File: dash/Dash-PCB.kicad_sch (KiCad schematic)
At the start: 91 parts, among them IC1 HT16K33, IC2 TLV62130ARGTT, J1 IO, J2 Conn_01x05_Pin, J3 Conn_02x06_Counter_Clockwise, Q1 XP262N7002TR-G, Q2 XP262N7002TR-G, Q3 XP262N7002TR-G, Q4 XP262N7002TR-G, U1 PIC18F47Q84-I/PT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

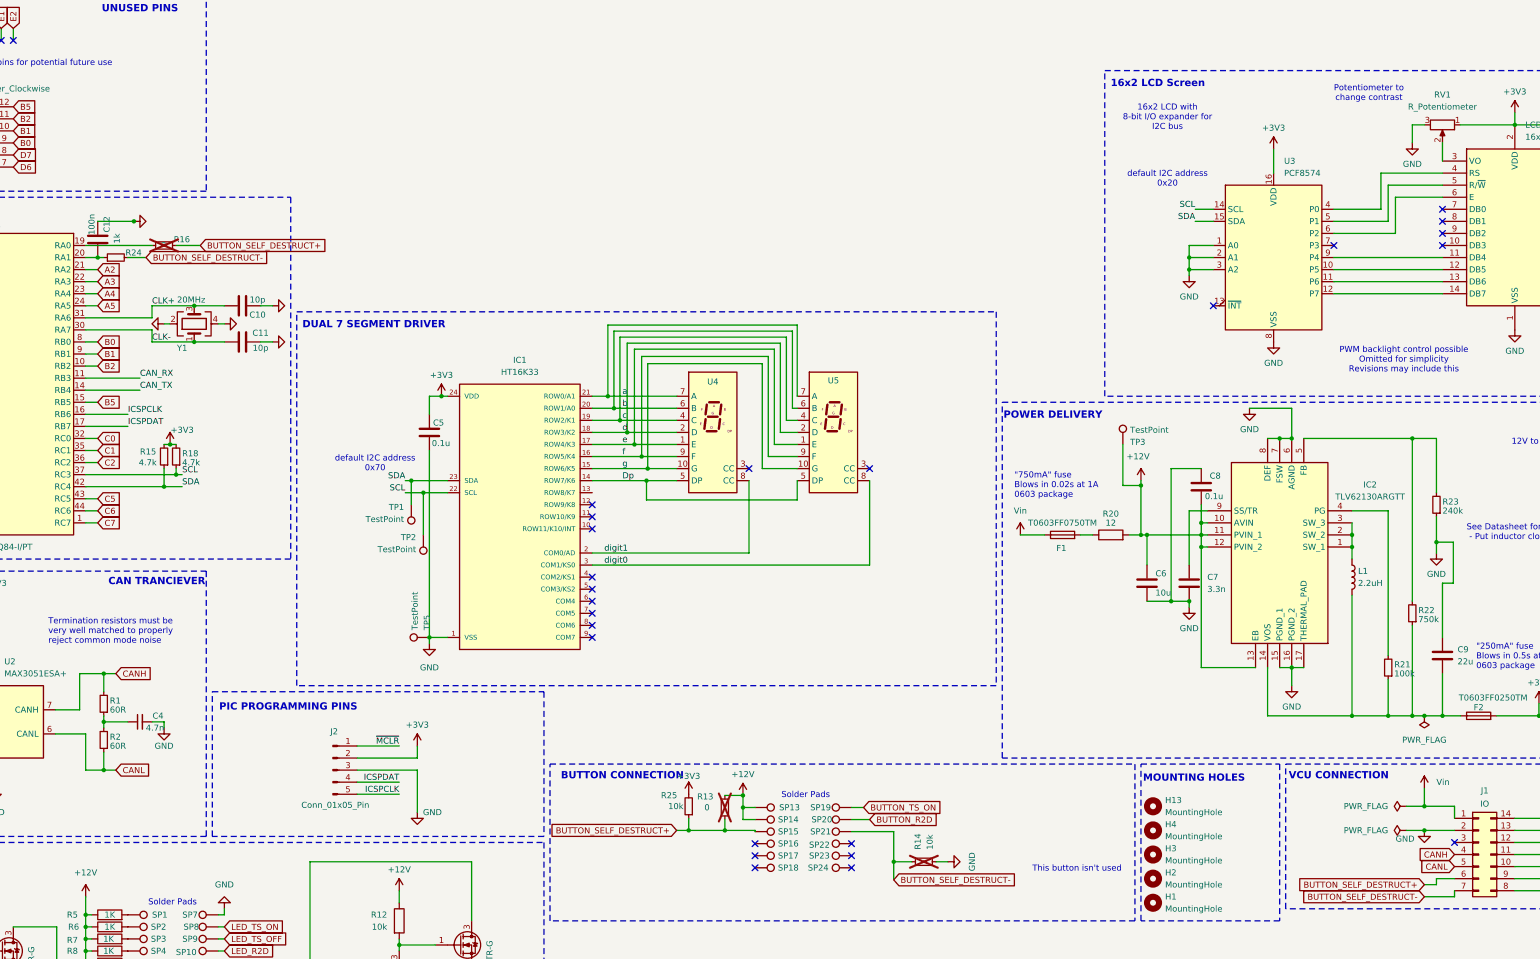
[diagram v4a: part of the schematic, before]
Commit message: Tweaked PCB
Moved CAN X-ver to back, neatened and shortened traces
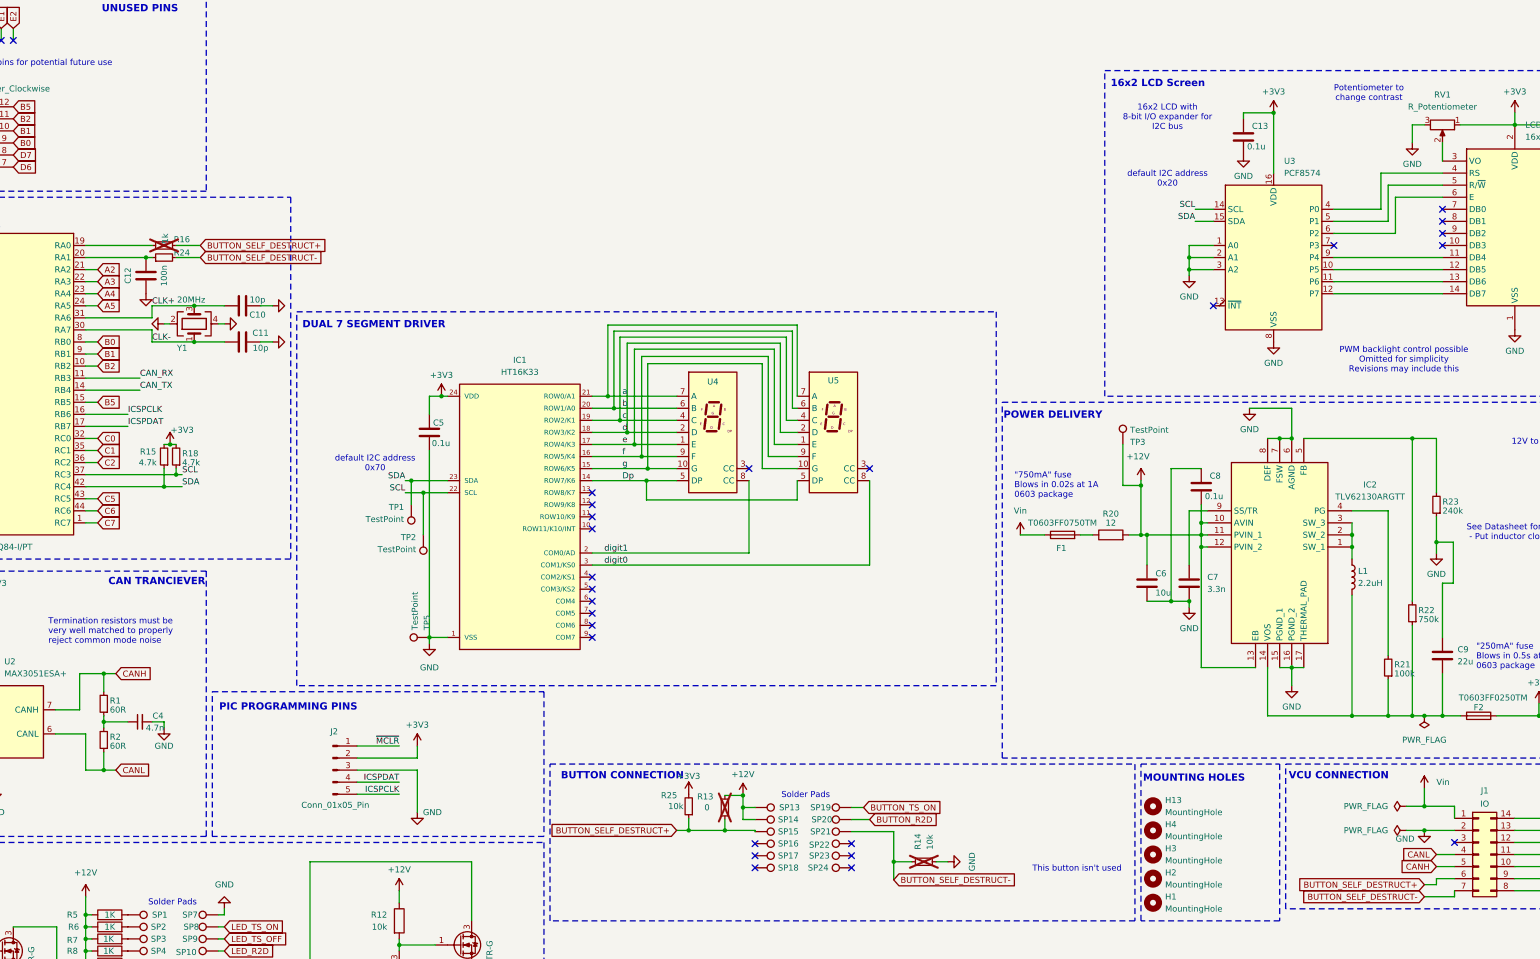
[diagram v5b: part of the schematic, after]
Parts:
- added C13: 0.1u, Capacitor_SMD:C_0805_2012Metric_Pad1.18x1.45mm_HandSolder, symbol Device:C
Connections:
- net +3V3: now also C13.1
- net CANH: now also J1.5 (Pin_5); no longer J1.4 (Pin_4)
- net CANL: now also J1.4 (Pin_4); no longer J1.5 (Pin_5)
- net GND: now also C13.2
- no-connect marks 42 -> 43
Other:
- moved on the sheet: C12, R24

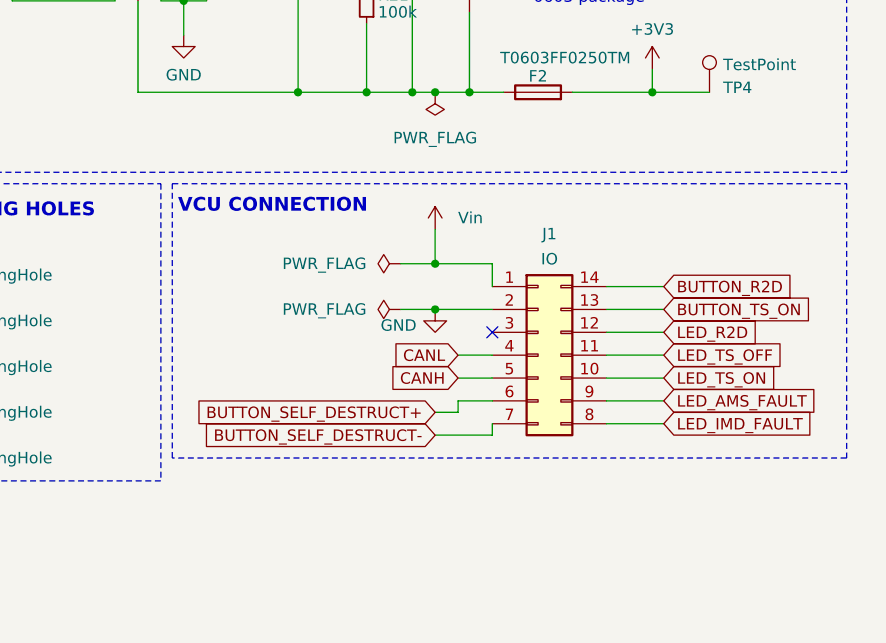
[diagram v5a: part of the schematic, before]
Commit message: button debounce circuit fixed and solder jumpers added
Solder jumpers added to self destruct button's vcu connection. This is because when the button is used for changing lcd information, it has nothing to do with the VCU so needs no connection. Also prevents the VCU accidentally damaging the dash board through these pins.

Also, minor silkscreen placement improvements.
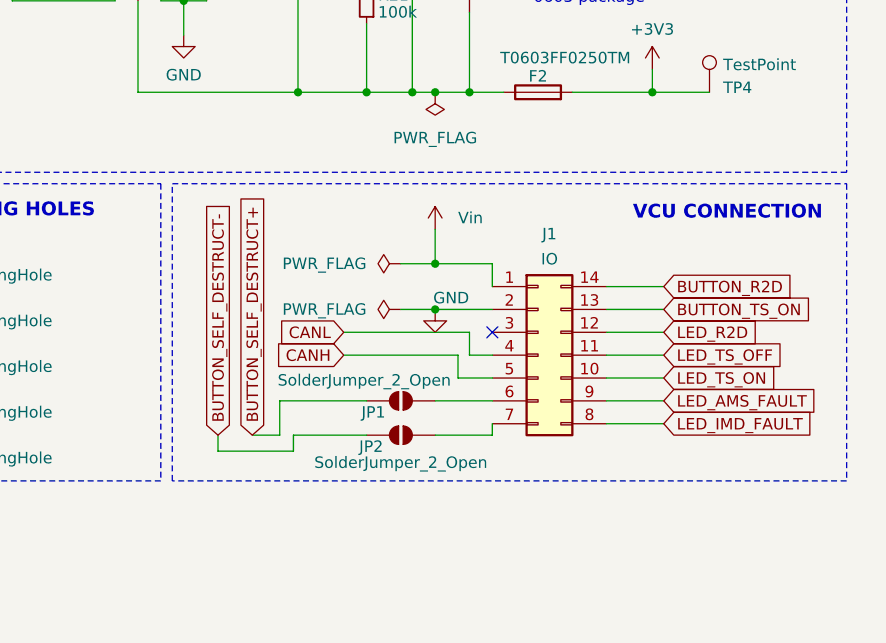
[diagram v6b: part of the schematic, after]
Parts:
- added JP1, JP2: SolderJumper_2_Open, symbol Jumper:SolderJumper_2_Open
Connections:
- net BUTTON_SELF_DESTRUCT+: now also JP1.1 (A); no longer J1.6 (Pin_6)
- net BUTTON_SELF_DESTRUCT-: now also JP2.1 (A); no longer J1.7 (Pin_7)
- new net: J1.6 (Pin_6), JP1.2 (B)
- new net: J1.7 (Pin_7), JP2.2 (B)

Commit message: forgot to commit schematic
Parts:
- JP1, JP2: footprint (none) -> Jumper:SolderJumper-2_P1.3mm_Open_TrianglePad1.0x1.5mm
- R14: value 10k -> 0; now fitted
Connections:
- net BUTTON_SELF_DESTRUCT+: now also R24.2; no longer R16.2
- net BUTTON_SELF_DESTRUCT-: now also R16.2; no longer R24.2
- net at U1.19 (RA0): now also C12.1, R24.1; no longer R16.1
- new net: R16.1, U1.20 (RA1)
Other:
- moved on the sheet: C12, R16, R24
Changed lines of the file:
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@@
 	)
 	(junction
+		(at 87.63 109.22)
+		(diameter 0)
+		(color 0 0 0 0)
+	)
+	(junction
 		(at 147.32 158.75)
 		(diameter 0)
@@
 	)
 	(junction
-		(at 91.44 111.76)
-		(diameter 0)
-		(color 0 0 0 0)
-	)
-	(junction
 		(at 194.31 151.13)
 		(diameter 0)
@@
 	(wire
 		(pts
-			(xy 97.79 109.22) (xy 102.87 109.22)
-		)
-		(stroke
-			(width 0)
-			(type default)
-		)
-	)
-	(wire
-		(pts
 			(xy 78.74 212.09) (xy 78.74 219.71)
 		)
@@
 	(wire
 		(pts
+			(xy 97.79 111.76) (xy 102.87 111.76)
+		)
+		(stroke
+			(width 0)
+			(type default)
+		)
+	)
+	(wire
+		(pts
 			(xy 228.6 125.984) (xy 188.722 125.984)
 		)
@@
 	(wire
 		(pts
-			(xy 97.79 111.76) (xy 102.87 111.76)
+			(xy 97.79 109.22) (xy 102.87 109.22)
 		)
 		(stroke
@@
 	(wire
 		(pts
-			(xy 78.74 109.22) (xy 92.71 109.22)
-		)
-		(stroke
-			(width 0)
-			(type default)
-		)
-	)
-	(wire
-		(pts
 			(xy 379.73 240.03) (xy 386.08 240.03)
 		)
@@
 	(wire
 		(pts
+			(xy 78.74 111.76) (xy 92.71 111.76)
+		)
+		(stroke
+			(width 0)
+			(type default)
+		)
+	)
+	(wire
+		(pts
 			(xy 38.1 125.73) (xy 40.64 125.73)
 		)
@@
 	(wire
 		(pts
+			(xy 87.63 109.22) (xy 92.71 109.22)
+		)
+		(stroke
+			(width 0)
+			(type default)
+		)
+	)
+	(wire
+		(pts
 			(xy 223.774 151.13) (xy 223.774 131.064)
 		)
@@
 	(wire
 		(pts
+			(xy 87.63 104.14) (xy 87.63 109.22)
+		)
+		(stroke
+			(width 0)
+			(type default)
+		)
+	)
+	(wire
+		(pts
 			(xy 364.49 208.28) (xy 368.3 208.28)
 		)
@@
 	(wire
 		(pts
+			(xy 78.74 109.22) (xy 87.63 109.22)
+		)
+		(stroke
+			(width 0)
+			(type default)
+		)
+	)
+	(wire
+		(pts
 			(xy 350.52 237.49) (xy 363.22 237.49)
 		)
@@
 	(wire
 		(pts
-			(xy 91.44 111.76) (xy 92.71 111.76)
-		)
-		(stroke
-			(width 0)
-			(type default)
-		)
-	)
-	(wire
-		(pts
 			(xy 358.14 208.28) (xy 360.68 208.28)
 		)
@@
 	(wire
 		(pts
-			(xy 78.74 111.76) (xy 91.44 111.76)
-		)
-		(stroke
-			(width 0)
-			(type default)
-		)
-	)
-	(wire
-		(pts
 			(xy 144.78 245.11) (xy 144.78 247.65)
 		)
@@
 		(in_bom yes)
 		(on_board yes)
-		(dnp yes)
+		(dnp no)
 		(fields_autoplaced yes)
 		(property "Reference" "R14"
@@
 			)
 		)
-		(property "Value" "10k"
+		(property "Value" "0"
 			(at 256.54 236.474 0)
 			(effects
@@
 			)
 		)
-		(property "Footprint" ""
+		(property "Footprint" "Jumper:SolderJumper-2_P1.3mm_Open_TrianglePad1.0x1.5mm"
 			(at 356.87 242.57 0)
 			(effects
@@
 	(symbol
 		(lib_id "Device:R_Small")
-		(at 95.25 109.22 90)
+		(at 95.25 111.76 90)
 		(unit 1)
 		(exclude_from_sim no)
@@
 		(dnp yes)
 		(property "Reference" "R16"
-			(at 97.282 107.95 90)
+			(at 97.282 110.49 90)
 			(effects
 				(font
@@
 		)
 		(property "Value" "0"
-			(at 95.25 108.458 0)
+			(at 95.25 110.998 0)
 			(effects
 				(font
@@
 		)
 		(property "Footprint" "Resistor_SMD:R_0805_2012Metric_Pad1.20x1.40mm_HandSolder"
-			(at 95.25 109.22 0)
+			(at 95.25 111.76 0)
 			(effects
 				(font
@@
 		)
 		(property "Datasheet" "~"
-			(at 95.25 109.22 0)
+			(at 95.25 111.76 0)
 			(effects
 				(font
@@
 		)
 		(property "Description" "Resistor, small symbol"
-			(at 95.25 109.22 0)
+			(at 95.25 111.76 0)
 			(effects
 				(font
@@
 	(symbol
 		(lib_id "Device:R_Small")
-		(at 95.25 111.76 90)
+		(at 95.25 109.22 90)
 		(unit 1)
 		(exclude_from_sim no)
@@
 		(dnp no)
 		(property "Reference" "R24"
-			(at 97.282 110.744 90)
+			(at 97.282 108.204 90)
 			(effects
 				(font
@@
 		)
 		(property "Value" "1k"
-			(at 95.504 106.68 0)
+			(at 95.504 104.14 0)
 			(effects
 				(font
@@
 		)
 		(property "Footprint" "Resistor_SMD:R_0805_2012Metric_Pad1.20x1.40mm_HandSolder"
-			(at 95.25 111.76 0)
+			(at 95.25 109.22 0)
 			(effects
 				(font
@@
 		)
 		(property "Datasheet" "~"
-			(at 95.25 111.76 0)
+			(at 95.25 109.22 0)
 			(effects
 				(font
@@
 		)
 		(property "Description" "Resistor, small symbol"
-			(at 95.25 111.76 0)
+			(at 95.25 109.22 0)
 			(effects
 				(font
@@
 	(symbol
 		(lib_id "power:GND")
-		(at 91.44 119.38 0)
+		(at 80.01 104.14 270)
 		(unit 1)
 		(exclude_from_sim no)
@@
 		(dnp no)
 		(property "Reference" "#PWR044"
-			(at 91.44 125.73 0)
+			(at 73.66 104.14 0)
 			(effects
 				(font
@@
 		)
 		(property "Value" "GND"
-			(at 88.9 121.92 90)
+			(at 77.47 101.6 90)
 			(effects
 				(font
@@
 		)
 		(property "Footprint" ""
-			(at 91.44 119.38 0)
+			(at 80.01 104.14 0)
 			(effects
 				(font
@@
 		)
 		(property "Datasheet" ""
-			(at 91.44 119.38 0)
+			(at 80.01 104.14 0)
 			(effects
 				(font
@@
 		)
 		(property "Description" ""
-			(at 91.44 119.38 0)
+			(at 80.01 104.14 0)
 			(effects
 				(font
@@
 	(symbol
 		(lib_id "Device:C")
-		(at 91.44 115.57 0)
+		(at 83.82 104.14 270)
 		(unit 1)
 		(exclude_from_sim no)
@@
 		(dnp no)
 		(property "Reference" "C12"
-			(at 87.63 115.57 90)
+			(at 83.82 100.33 90)
 			(effects
 				(font
@@
 		)
 		(property "Value" "100n"
-			(at 95.25 115.57 90)
+			(at 83.82 107.95 90)
 			(effects
 				(font
@@
 		)
 		(property "Footprint" "Capacitor_SMD:C_0603_1608Metric_Pad1.08x0.95mm_HandSolder"
-			(at 92.4052 119.38 0)
+			(at 80.01 105.1052 0)
 			(effects
 				(font
@@
 		)
 		(property "Datasheet" "~"
-			(at 91.44 115.57 0)
+			(at 83.82 104.14 0)
 			(effects
 				(font
@@
 		)
 		(property "Description" ""
-			(at 91.44 115.57 0)
+			(at 83.82 104.14 0)
 			(effects
 				(font
@@
 		)
 		(property "Manufacturer_Part_Number" "C0805C100J1RACAUTO"
-			(at 91.44 115.57 0)
+			(at 83.82 104.14 0)
 			(effects
 				(font
@@
 		)
 		(property "Mouser Part Number" "80-C0805C100J1RAUTO "
-			(at 91.44 115.57 0)
+			(at 83.82 104.14 0)
 			(effects
 				(font
@@
 			)
 		)
-		(property "Footprint" ""
+		(property "Footprint" "Jumper:SolderJumper-2_P1.3mm_Open_TrianglePad1.0x1.5mm"
 			(at 356.87 246.38 0)
 			(effects
@@
 		(dnp no)
 		(fields_autoplaced yes)
-		(property "Reference" "#PWR45"
+		(property "Reference" "#PWR045"
 			(at 322.58 96.52 0)
 			(effects
@@
 			(project "Dash-PCB"
 				(path "/8bd0bf3b-367d-470a-bc4a-b460b6479d15"
-					(reference "#PWR45")
+					(reference "#PWR045")
 					(unit 1)
 				)

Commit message: minor layout tweaks
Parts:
- J1: symbol Connector_Generic:Conn_02x07_Counter_Clockwise -> Connector_Generic_MountingPin:Conn_02x07_Counter_Clockwise_MountingPin
- JP1, JP2: footprint Jumper:SolderJumper-2_P1.3mm_Open_TrianglePad1.0x1.5mm -> Jumper:SolderJumper-2_P1.3mm_Open_RoundedPad1.0x1.5mm
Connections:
- net GND: now also J1.MP (MountPin)
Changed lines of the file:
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@@
 	(label "CAN_TX"
 		(at 90.17 139.7 0)
-		(fields_autoplaced yes)
 		(effects
 			(font
@@
 	(label "digit0"
 		(at 187.96 176.53 0)
-		(fields_autoplaced yes)
 		(effects
 			(font
@@
 	(label "CLK-"
 		(at 92.71 129.54 0)
-		(fields_autoplaced yes)
 		(effects
 			(font
@@
 	(label "c"
 		(at 191.77 146.05 0)
-		(fields_autoplaced yes)
 		(effects
 			(font
@@
 	(label "CAN_TX"
 		(at 31.75 204.47 0)
-		(fields_autoplaced yes)
 		(effects
 			(font
@@
 	(label "SDA"
 		(at 312.42 104.14 180)
-		(fields_autoplaced yes)
 		(effects
 			(font
@@
 	(label "CAN_RX"
 		(at 90.17 137.16 0)
-		(fields_autoplaced yes)
 		(effects
 			(font
@@
 	(label "SDA"
 		(at 146.05 158.75 180)
-		(fields_autoplaced yes)
 		(effects
 			(font
@@
 	(label "SCL"
 		(at 99.06 157.48 0)
-		(fields_autoplaced yes)
 		(effects
 			(font
@@
 	(label "CLK+"
 		(at 92.71 121.92 0)
-		(fields_autoplaced yes)
 		(effects
 			(font
@@
 	(label "ICSPCLK"
 		(at 144.78 224.79 180)
-		(fields_autoplaced yes)
 		(effects
 			(font
@@
 	(label "SDA"
 		(at 99.06 160.02 0)
-		(fields_autoplaced yes)
 		(effects
 			(font
@@
 	(label "ICSPDAT"
 		(at 87.63 147.32 0)
-		(fields_autoplaced yes)
 		(effects
 			(font
@@
 	(label "a"
 		(at 191.77 140.97 0)
-		(fields_autoplaced yes)
 		(effects
 			(font
@@
 	(label "SCL"
 		(at 146.05 161.29 180)
-		(fields_autoplaced yes)
 		(effects
 			(font
@@
 	(label "g"
 		(at 191.77 156.21 0)
-		(fields_autoplaced yes)
 		(effects
 			(font
@@
 	(label "CAN_RX"
 		(at 31.75 207.01 0)
-		(fields_autoplaced yes)
 		(effects
 			(font
@@
 	(label "b"
 		(at 191.77 143.51 0)
-		(fields_autoplaced yes)
 		(effects
 			(font
@@
 	(label "ICSPDAT"
 		(at 144.78 222.25 180)
-		(fields_autoplaced yes)
 		(effects
 			(font
@@
 	(label "e"
 		(at 191.77 151.13 0)
-		(fields_autoplaced yes)
 		(effects
 			(font
@@
 	(label "digit1"
 		(at 187.96 173.99 0)
-		(fields_autoplaced yes)
 		(effects
 			(font
@@
 	(label "Dp"
 		(at 191.77 158.75 0)
-		(fields_autoplaced yes)
 		(effects
 			(font
@@
 	(label "ICSPCLK"
 		(at 87.63 144.78 0)
-		(fields_autoplaced yes)
 		(effects
 			(font
@@
 	(label "SCL"
 		(at 312.42 101.6 180)
-		(fields_autoplaced yes)
 		(effects
 			(font
@@
 	(label "d"
 		(at 191.77 148.59 0)
-		(fields_autoplaced yes)
 		(effects
 			(font
@@
 	(label "~{MCLR}"
 		(at 25.4 158.75 0)
-		(fields_autoplaced yes)
 		(effects
 			(font
@@
 	(label "f"
 		(at 191.77 153.67 0)
-		(fields_autoplaced yes)
 		(effects
 			(font
@@
 	(label "~{MCLR}"
 		(at 144.78 214.63 180)
-		(fields_autoplaced yes)
 		(effects
 			(font
@@
 			)
 		)
-		(property "Footprint" "Jumper:SolderJumper-2_P1.3mm_Open_TrianglePad1.0x1.5mm"
+		(property "Footprint" "Jumper:SolderJumper-2_P1.3mm_Open_RoundedPad1.0x1.5mm"
 			(at 356.87 242.57 0)
 			(effects
@@
 	)
 	(symbol
-		(lib_id "Connector_Generic:Conn_02x07_Counter_Clockwise")
+		(lib_id "Connector_Generic_MountingPin:Conn_02x07_Counter_Clockwise_MountingPin")
 		(at 372.11 237.49 0)
 		(unit 1)
@@
 			)
 		)
-		(property "Description" "Generic connector, double row, 02x07, counter clockwise pin numbering scheme (similar to DIP package numbering), script generated (kicad-library-utils/schlib/autogen/connector/)"
+		(property "Description" "Generic connectable mounting pin connector, double row, 02x07, counter clockwise pin numbering scheme (similar to DIP package numbering), script generated (kicad-library-utils/schlib/autogen/connector/)"
 			(at 372.11 237.49 0)
 			(effects
@@
 		(pin "9"
 		)
+		(pin "MP"
+		)
 		(instances
 			(project ""
@@
 			)
 		)
-		(property "Footprint" "Jumper:SolderJumper-2_P1.3mm_Open_TrianglePad1.0x1.5mm"
+		(property "Footprint" "Jumper:SolderJumper-2_P1.3mm_Open_RoundedPad1.0x1.5mm"
 			(at 356.87 246.38 0)
 			(effects
@@
 					(unit 1)
 				)
+			)
+		)
+	)
+	(symbol
+		(lib_id "power:GND")
+		(at 373.38 250.19 0)
+		(unit 1)
+		(exclude_from_sim no)
+		(in_bom yes)
+		(on_board yes)
+		(dnp no)
+		(property "Reference" "#PWR46"
+			(at 373.38 256.54 0)
+			(effects
+				(font
+					(size 1.27 1.27)
+				)
+				(hide yes)
+			)
+		)
+		(property "Value" "GND"
+			(at 375.158 248.92 0)
+			(effects
+				(font
+					(size 1.27 1.27)
+				)
+			)
+		)
+		(property "Footprint" ""
+			(at 373.38 250.19 0)
+			(effects
+				(font
+					(size 1.27 1.27)
+				)
+				(hide yes)
+			)
+		)
+		(property "Datasheet" ""
+			(at 373.38 250.19 0)
+			(effects
+				(font
+					(size 1.27 1.27)
+				)
+				(hide yes)
+			)
+		)
+		(property "Description" "Power symbol creates a global label with name \"GND\" , ground"
+			(at 373.38 250.19 0)
+			(effects
+				(font
+					(size 1.27 1.27)
+				)
+				(hide yes)
+			)
+		)
+		(pin "1"
+		)
+		(instances
+			(project "Dash-PCB"
+				(path "/8bd0bf3b-367d-470a-bc4a-b460b6479d15"
+					(reference "#PWR46")
+					(unit 1)
+				)
